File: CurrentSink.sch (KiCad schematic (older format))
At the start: 3 parts, among them J101 Test-Source, J102 Power-Jumper, J103 Power-Connector

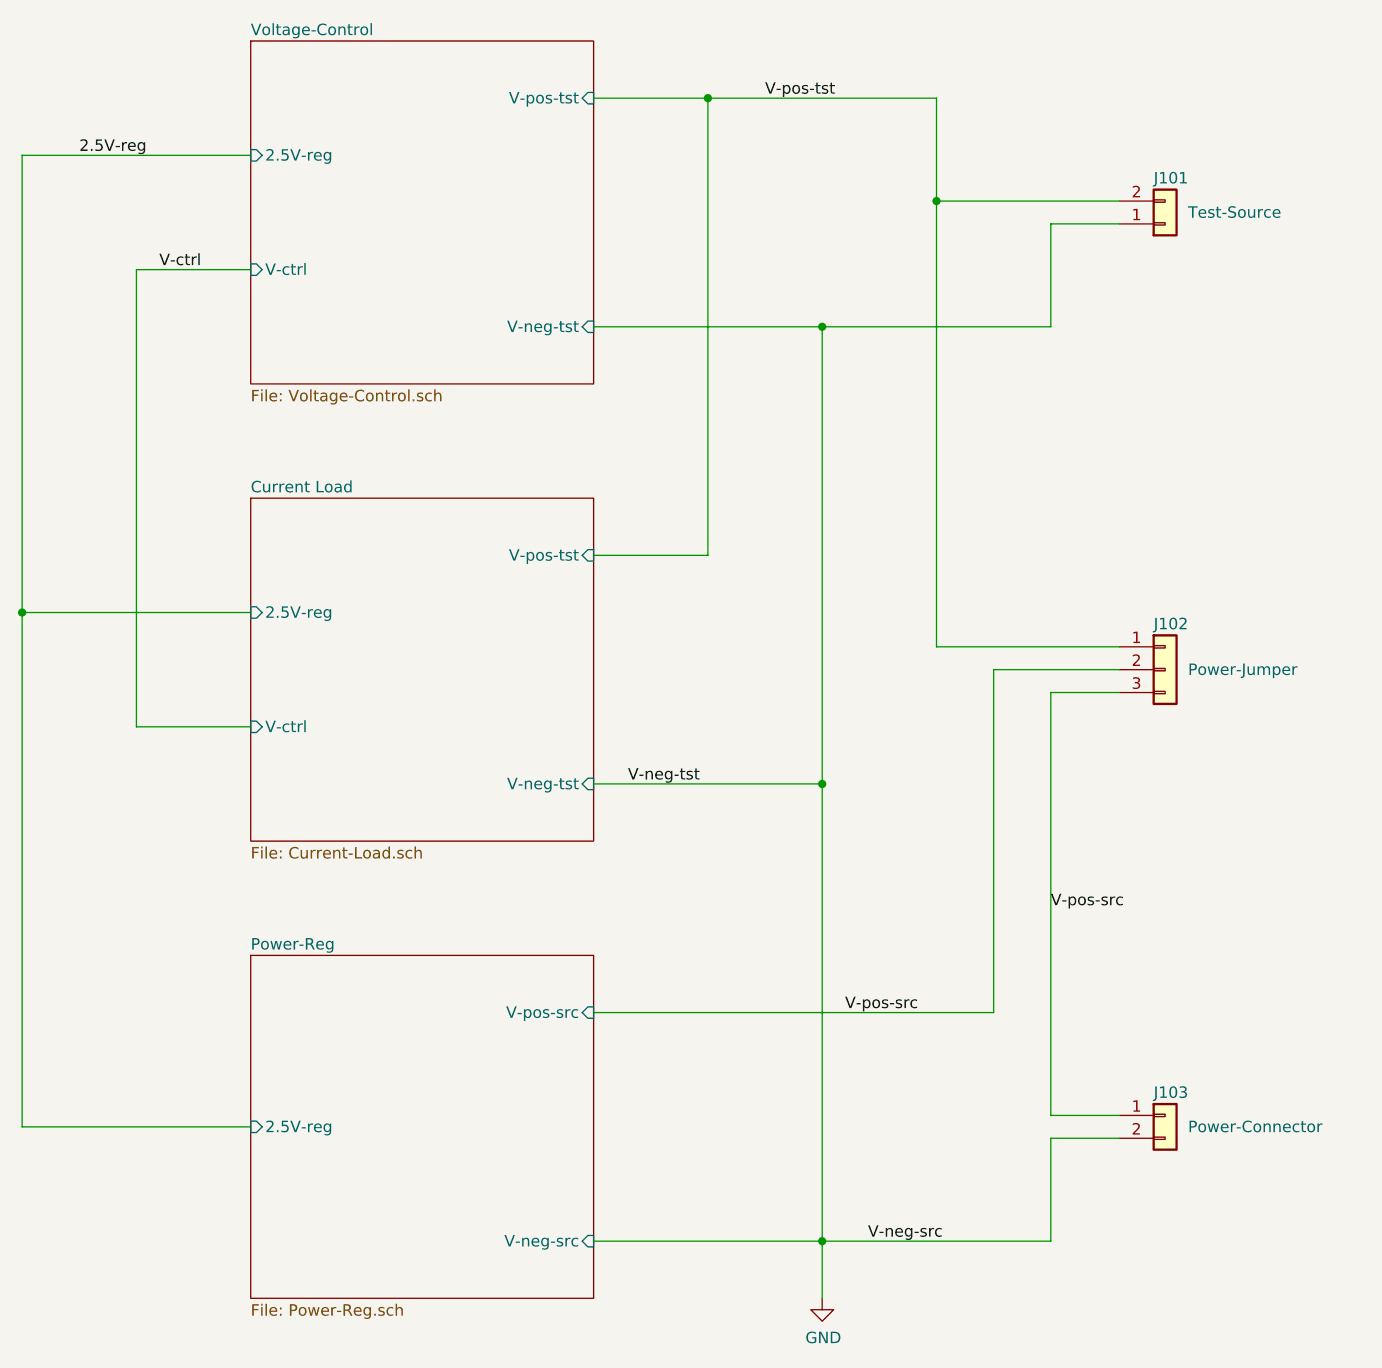
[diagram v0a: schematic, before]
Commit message: PCB completed with Op-Amp mounted horizontally
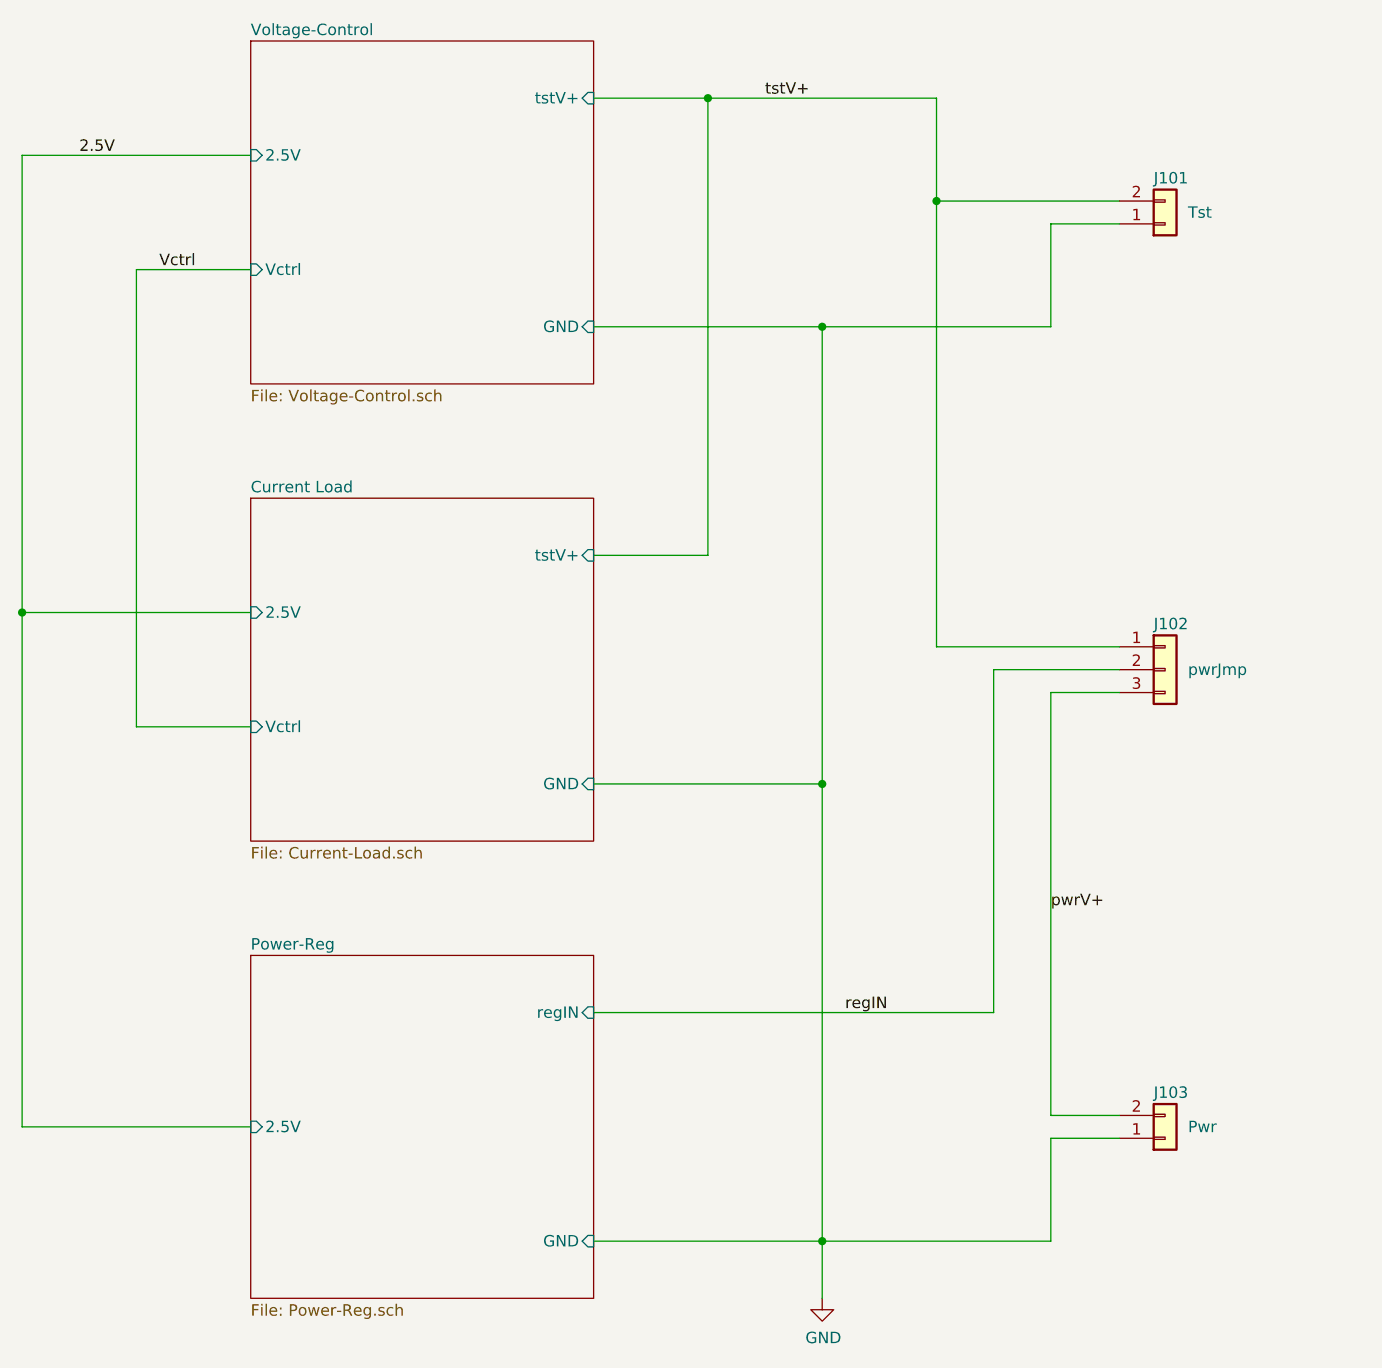
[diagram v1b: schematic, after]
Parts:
- J101: value Test-Source -> Tst; footprint Connector_PinHeader_1.27mm:PinHeader_1x02_P1.27mm_Vertical -> TerminalBlock_Phoenix:TerminalBlock_Phoenix_PT-1,5-2-3.5-H_1x02_P3.50mm_Horizontal; MPN (none) -> 1984617
- J102: value Power-Jumper -> pwrJmp
- J103: value Power-Connector -> Pwr; footprint Connector_BarrelJack:BarrelJack_CUI_PJ-036AH-SMT_Horizontal -> TerminalBlock_Phoenix:TerminalBlock_Phoenix_PT-1,5-2-3.5-H_1x02_P3.50mm_Horizontal; MPN (none) -> 1984617
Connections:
- net GND: now also J103.1 (Pin_1); no longer J103.2 (Pin_2)
- removed net V-pos-src: J102.2 (Pin_2), J102.3 (Pin_3), J103.1 (Pin_1)
- net V-pos-tst renamed tstV+
- new net pwrV+: J102.3 (Pin_3), J103.2 (Pin_2)
- new net regIN: J102.2 (Pin_2)
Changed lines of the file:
@@
 P 6500 1800
 F 0 "J101" H 6450 1600 50  0000 L CNN
-F 1 "Test-Source" H 6600 1750 50  0000 L CNN
-F 2 "Connector_PinHeader_1.27mm:PinHeader_1x02_P1.27mm_Vertical" H 6500 1800 50  0001 C CNN
-F 3 "~" H 6500 1800 50  0001 C CNN
+F 1 "Tst" H 6600 1750 50  0000 L CNN
+F 2 "TerminalBlock_Phoenix:TerminalBlock_Phoenix_PT-1,5-2-3.5-H_1x02_P3.50mm_Horizontal" H 6500 1800 50  0001 C CNN
+F 3 "https://media.digikey.com/pdf/Data%20Sheets/Phoenix%20Contact%20PDFs/Combicon%20Compact%20Series.pdf" H 6500 1800 50  0001 C CNN
+F 4 "1984617" H 6500 1800 50  0001 C CNN "MPN"
 	1    6500 1800
 	1    0    0    1
@@
 F0 "Voltage-Control" 50
 F1 "Voltage-Control.sch" 50
-F2 "V-neg-tst" I R 4000 2250 50
-F3 "V-pos-tst" I R 4000 1250 50
-F4 "V-ctrl" I L 2500 2000 50
-F5 "2.5V-reg" I L 2500 1500 50
+F2 "tstV+" I R 4000 1250 50
+F3 "Vctrl" I L 2500 2000 50
+F4 "2.5V" I L 2500 1500 50
+F5 "GND" I R 4000 2250 50
 $EndSheet
 $Comp
 L Connector_Generic:Conn_01x02 J103
 U 1 1 60184A6A
-P 6500 5700
-F 0 "J103" H 6450 5800 50  0000 L CNN
-F 1 "Power-Connector" H 6600 5650 50  0000 L CNN
-F 2 "Connector_BarrelJack:BarrelJack_CUI_PJ-036AH-SMT_Horizontal" H 6500 5700 50  0001 C CNN
-F 3 "~" H 6500 5700 50  0001 C CNN
-	1    6500 5700
-	1    0    0    -1
+P 6500 5800
+F 0 "J103" H 6450 5600 50  0000 L CNN
+F 1 "Pwr" H 6600 5750 50  0000 L CNN
+F 2 "TerminalBlock_Phoenix:TerminalBlock_Phoenix_PT-1,5-2-3.5-H_1x02_P3.50mm_Horizontal" H 6500 5800 50  0001 C CNN
+F 3 "https://media.digikey.com/pdf/Data%20Sheets/Phoenix%20Contact%20PDFs/Combicon%20Compact%20Series.pdf" H 6500 5800 50  0001 C CNN
+F 4 "1984617" H 6500 5800 50  0001 C CNN "MPN"
+	1    6500 5800
+	1    0    0    1
 $EndComp
 $Sheet
@@
 F0 "Current Load" 50
 F1 "Current-Load.sch" 50
-F2 "V-ctrl" I L 2500 4000 50
-F3 "V-pos-tst" I R 4000 3250 50
-F4 "V-neg-tst" I R 4000 4250 50
-F5 "2.5V-reg" I L 2500 3500 50
+F2 "Vctrl" I L 2500 4000 50
+F3 "tstV+" I R 4000 3250 50
+F4 "2.5V" I L 2500 3500 50
+F5 "GND" I R 4000 4250 50
 $EndSheet
 $Sheet
@@
 F0 "Power-Reg" 50
 F1 "Power-Reg.sch" 50
-F2 "2.5V-reg" I L 2500 5750 50
-F3 "V-neg-src" I R 4000 6250 50
-F4 "V-pos-src" I R 4000 5250 50
+F2 "2.5V" I L 2500 5750 50
+F3 "regIN" I R 4000 5250 50
+F4 "GND" I R 4000 6250 50
 $EndSheet
 Wire Wire Line
@@
 AR Path="/601B7636/60184A04" Ref="J?"  Part="1"
 F 0 "J102" H 6450 3950 50  0000 L CNN
-F 1 "Power-Jumper" H 6600 3750 50  0000 L CNN
+F 1 "pwrJmp" H 6600 3750 50  0000 L CNN
 F 2 "Connector_PinHeader_1.27mm:PinHeader_1x03_P1.27mm_Vertical" H 6500 3750 50  0001 C CNN
 F 3 "~" H 6500 3750 50  0001 C CNN
@@
 Wire Wire Line
 	2000 2000 2500 2000
-Text Label 5200 6250 0    50   ~ 0
-V-neg-src
+Text Label 5100 5250 0    50   ~ 0
+regIN
+Text Label 4750 1250 0    50   ~ 0
+tstV+
+Text Label 2100 2000 0    50   ~ 0
+Vctrl
+Text Label 1750 1500 0    50   ~ 0
+2.5V
 Text Label 6000 4800 0    50   ~ 0
-V-pos-src
-Text Label 5100 5250 0    50   ~ 0
-V-pos-src
-Text Label 4150 4250 0    50   ~ 0
-V-neg-tst
-Text Label 4750 1250 0    50   ~ 0
-V-pos-tst
-Text Label 2100 2000 0    50   ~ 0
-V-ctrl
-Text Label 1750 1500 0    50   ~ 0
-2.5V-reg
+pwrV+
 $EndSCHEMATC

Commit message: Fixed reversed Op-Amp for voltage limiting and potentiometer connections to allow for full range of the potentiometer.
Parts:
- J102: footprint Connector_PinHeader_1.27mm:PinHeader_1x03_P1.27mm_Vertical -> Connector_PinHeader_2.54mm:PinHeader_1x03_P2.54mm_Vertical
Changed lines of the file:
@@
 F 0 "J102" H 6450 3950 50  0000 L CNN
 F 1 "pwrJmp" H 6600 3750 50  0000 L CNN
-F 2 "Connector_PinHeader_1.27mm:PinHeader_1x03_P1.27mm_Vertical" H 6500 3750 50  0001 C CNN
+F 2 "Connector_PinHeader_2.54mm:PinHeader_1x03_P2.54mm_Vertical" H 6500 3750 50  0001 C CNN
 F 3 "~" H 6500 3750 50  0001 C CNN
 	1    6500 3750
